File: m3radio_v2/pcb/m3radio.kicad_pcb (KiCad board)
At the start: 2 copper layers, 40 x 40 mm, 61 parts, among them IC1 NCP380, IC101 STM32F405RxTx, IC102 MCP2562, IC103 MAX-7Q, IC201 Si4460, J101 WEST TOP, J102 WEST BOT, J103 EAST TOP, J104 EAST BOT, P101 COAX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

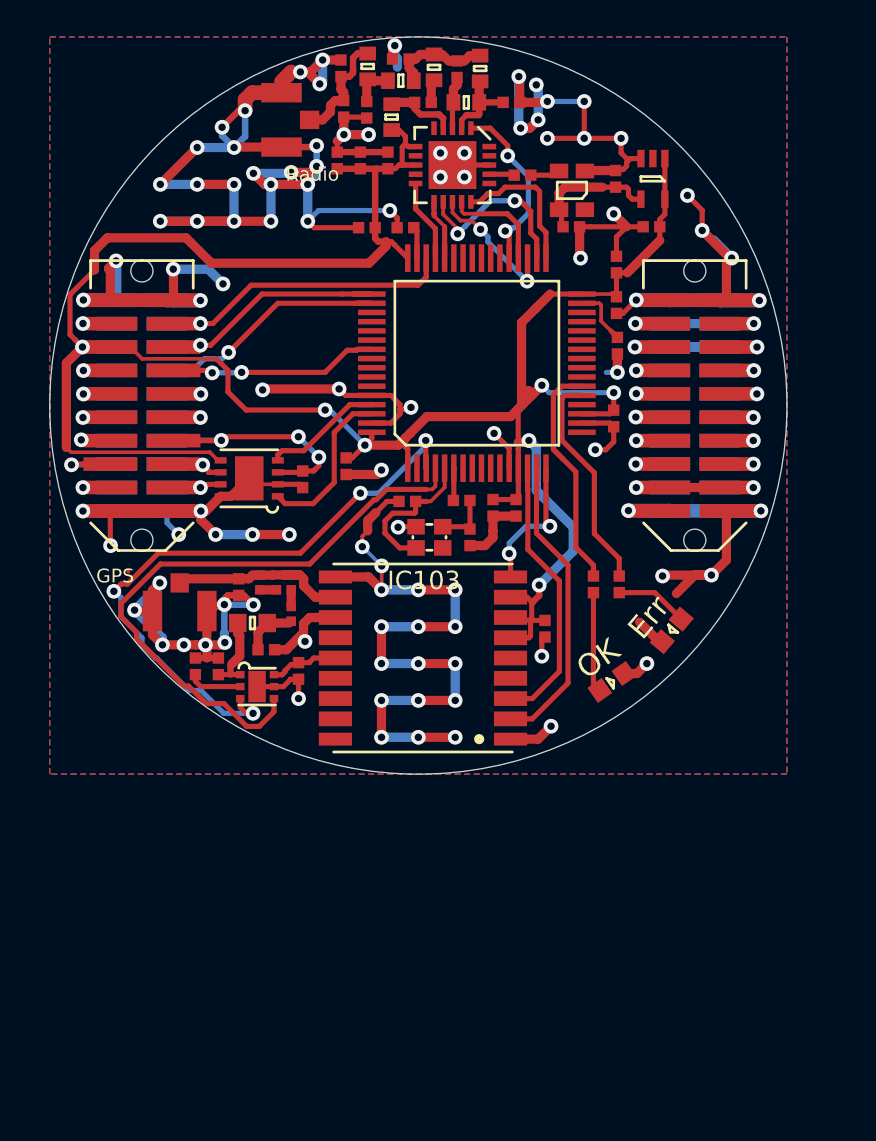
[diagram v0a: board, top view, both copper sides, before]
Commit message: Finish schematic, begin routing
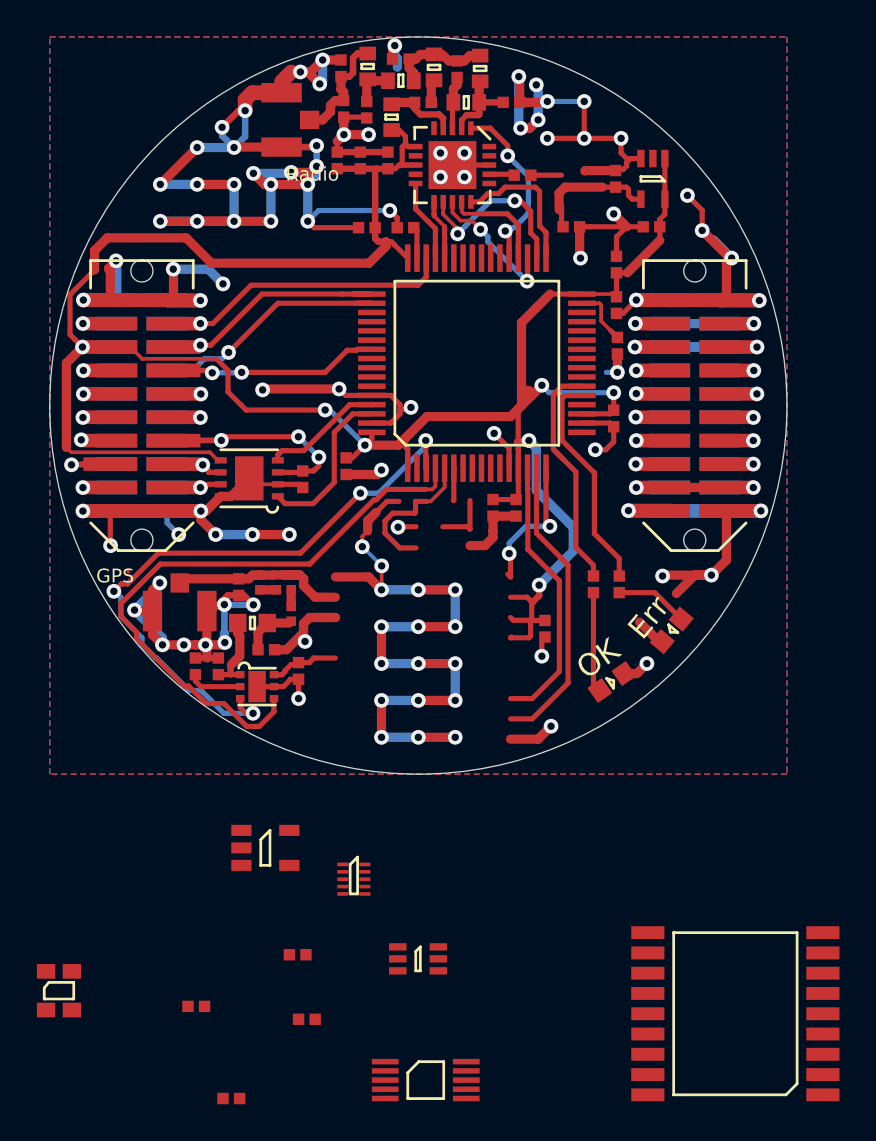
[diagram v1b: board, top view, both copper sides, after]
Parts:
- removed C101, C102: 10p, agg:0402
- removed IC103: MAX-7Q, M3radio:MAX-7Q
- removed R101: 100, agg:0402
- removed Y101: 26M, agg:XTAL-20x16
- removed Y201: TCXO, agg:TG-5006CG
- added C10: 100n, agg:0402, F.Cu at (93.5, 129.8)
- added C11: 1n, agg:0402, F.Cu at (94.0, 133.3)
- added C9: 100n, agg:0402, F.Cu at (89.8, 137.6)
- added IC2: NC7SZ04, agg:SOT-23-5, F.Cu at (91.7, 124.0)
- added IC3: CS2100-CP, agg:MSOP-10, F.Cu at (100.4, 136.6)
- added IC4: SL18860DC, agg:DFN-10-SL18860DC, F.Cu at (96.5, 125.7)
- added IC5: MAX_M8Q, agg:MAX-M8Q, F.Cu at (117.2, 133.0)
- added IC6: SN74LVC1G0832, agg:SC-70-6, F.Cu at (100.0, 130.0)
- added R3: 1M, agg:0402, F.Cu at (88.0, 132.6)
- added Y1: TCXO, agg:TG-5006CG, F.Cu at (80.5, 131.8)
- C1, C113: value 100nF -> 100n
- C106: value 1µ -> 1u
- C2, C3, C7, C8: value 1uF -> 1u
- C203: value 3pF -> 3p
- C204: value 36pF -> 36p
- C205: value 1.2pF -> 1.2p
- C206: value 3.3pF -> 3.3p
- C207: value 10pF -> 10p
- C208: value 4.7pF -> 4.7p
- C4: value 10nF -> 100n
- C5: value 100pF -> 1n
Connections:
- IC101 pad 2: Net-(IC101-Pad2) -> /GPS_PPS
- IC101 pad 29: Net-(IC101-Pad29) -> /PLL_SCL
- IC101 pad 30: Net-(IC101-Pad30) -> /PLL_SDA
- IC101 pad 33: /Radio/Radio_nSEL -> /Radio_nSEL
- IC101 pad 38: Net-(IC101-Pad38) -> /Radio_GATE
- IC101 pad 5: Net-(C101-Pad2) -> /STM_HSE
- IC201 pad 17: Net-(C5-Pad1) -> /Radio/Radio_XIN
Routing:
- net (no net): track 0.04 -> 44.0 mm, vias 0 -> 19
- net GND: track 329.0 -> 288.1 mm, vias 99 -> 80
- net Net-(C101-Pad2): track 8.06 -> 0.00 mm
- net /STM_HSE: track 0.00 -> 8.06 mm
- net Net-(C102-Pad1): track 3.08 -> 0.00 mm
- net /Radio_nSEL: track 0.00 -> 1.39 mm
- net /Radio/Radio_nSEL: track 7.92 -> 6.53 mm
- net Net-(C5-Pad1): track 1.37 -> 0.07 mm
- net /Radio/Radio_XIN: track 0.00 -> 1.30 mm

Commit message: Initial component placement (pcb)
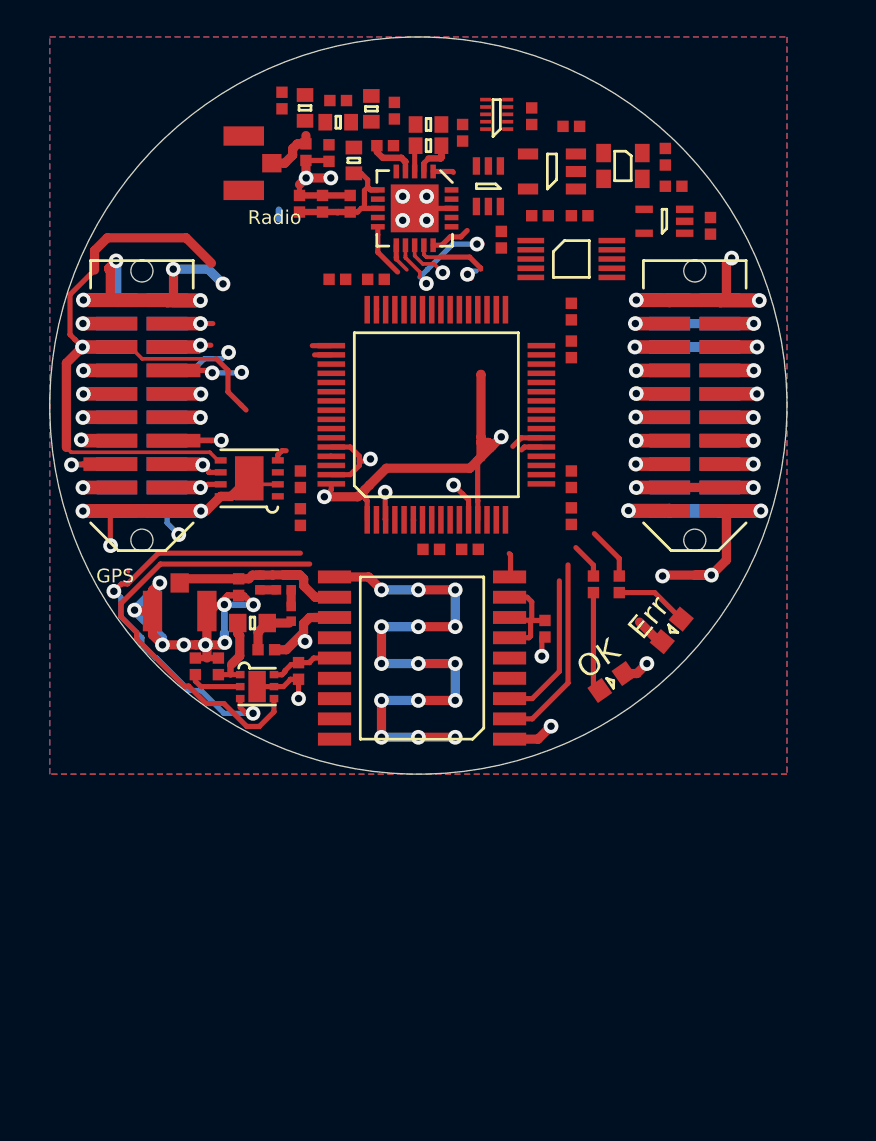
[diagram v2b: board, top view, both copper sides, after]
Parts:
- moved Y1 54.2 mm to (111.1, 87.0), turned to 270 degrees
- moved R3 51.9 mm to (108.3, 84.8), turned to 180 degrees
- moved C9 48.8 mm to (104.5, 91.0), turned to 270 degrees
- moved C10 47.2 mm to (106.2, 84.3), turned to 90 degrees
- moved C11 45.4 mm to (106.6, 89.7), turned to 180 degrees
- moved IC3 45.2 mm to (108.3, 92.0)
- moved IC4 42.2 mm to (104.2, 84.2), turned to 180 degrees
- moved IC6 42.1 mm to (103.8, 88.1), turned to 270 degrees
- moved IC2 39.9 mm to (107.2, 87.3), turned to 180 degrees
- moved IC5 25.7 mm to (100.2, 113.7)
- moved C103 13.9 mm to (108.3, 106.0), turned to 90 degrees
- moved C4 5.97 mm to (113.8, 88.1)
- moved L203 4.13 mm to (100.5, 84.8), turned to 180 degrees
- moved L206 4.08 mm to (93.8, 83.8)
- moved C205 4.08 mm to (98.7, 84.0)
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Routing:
- net GND: track 288.1 -> 194.4 mm, vias 80 -> 52
- net 3v3: track 139.0 -> 78.1 mm, vias 7 -> 3
- net (no net): track 44.0 -> 0.88 mm, vias 19 -> 1
- net /JTMS: track 17.6 -> 3.95 mm
- net /JTCK: track 13.5 -> 3.59 mm
- net /ANT_~EN: track 33.4 -> 23.9 mm
- net /LED_GRN: track 13.1 -> 3.68 mm
- net /ANT_~FLAG: track 34.4 -> 25.2 mm, vias 4 -> 3
- net /JTDI: track 14.3 -> 5.39 mm
- net /CAN_TXD: track 8.88 -> 0.00 mm
- net /Radio/Radio_SDN: track 9.81 -> 1.12 mm, vias 2 -> 0
- net /5v_CAN: track 14.2 -> 5.84 mm, vias 3 -> 1
- net /LED_RED: track 12.1 -> 4.00 mm
- net /STM_HSE: track 8.06 -> 0.00 mm
- net /JTDO: track 11.3 -> 3.76 mm
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
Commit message: Revise component placement
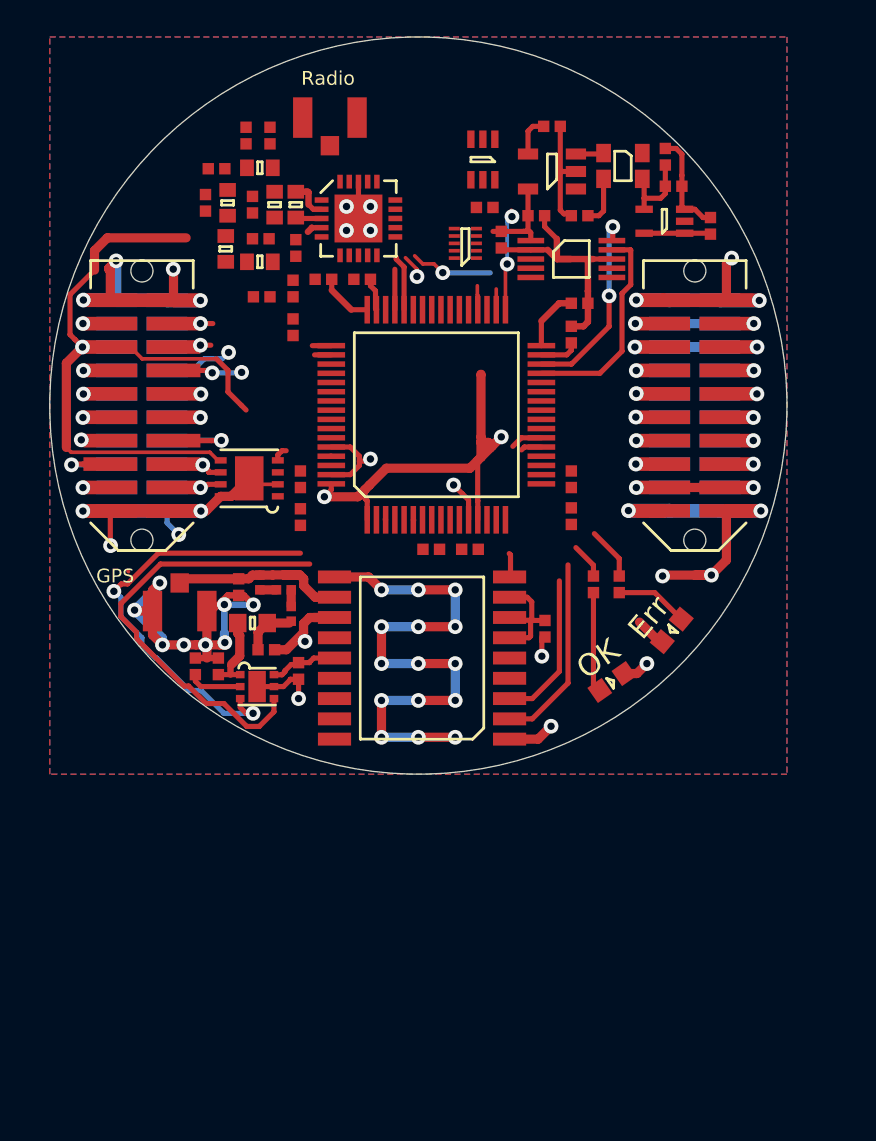
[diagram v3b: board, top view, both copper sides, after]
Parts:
- moved C203 12.0 mm to (91.0, 89.1)
- moved L204 10.3 mm to (91.4, 92.2), turned to 180 degrees
- moved C205 10.0 mm to (91.5, 91.0), turned to 180 degrees
- moved L203 9.42 mm to (92.2, 89.1), turned to 270 degrees
- moved C206 9.09 mm to (88.5, 89.0), turned to 90 degrees
- moved L201 8.45 mm to (89.5, 91.5), turned to 270 degrees
- moved L202 7.88 mm to (93.3, 89.1), turned to 90 degrees
- moved L205 7.43 mm to (89.7, 89.0), turned to 90 degrees
- moved C204 7.37 mm to (93.3, 91.5), turned to 270 degrees
- moved IC4 7.20 mm to (102.5, 91.2)
- moved C6 6.71 mm to (93.2, 95.8), turned to 270 degrees
- moved C207 6.16 mm to (89.0, 87.2), turned to 180 degrees
- moved C201 6.03 mm to (91.5, 94.1), turned to 180 degrees
- moved C10 5.57 mm to (103.6, 89.2), turned to 180 degrees
- moved C202 5.55 mm to (93.2, 93.7)
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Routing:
- net /PLL_SCL: track 0.00 -> 11.6 mm
- net /PLL_SDA: track 0.00 -> 10.8 mm, vias 0 -> 2
- net GND: track 194.4 -> 204.1 mm, vias 52 -> 49
- net Net-(C5-Pad1): track 0.00 -> 6.12 mm
- net /Radio_nSEL: track 0.00 -> 5.56 mm, vias 0 -> 2
- net 3v3: track 78.1 -> 83.6 mm
- net 1v8: track 0.00 -> 4.50 mm
- net /Radio/Radio_SCLK: track 6.22 -> 2.40 mm, vias 2 -> 1
- net Net-(C208-Pad1): track 2.94 -> 0.00 mm
- net Net-(C5-Pad2): track 0.00 -> 2.70 mm
- net /Radio/Radio_SDI: track 3.93 -> 1.31 mm
- net /Radio/TX_pin: track 2.78 -> 0.48 mm
- net Net-(IC2-Pad4): track 0.00 -> 2.20 mm
- net /Radio/Radio_nSEL: track 2.18 -> 0.00 mm
- net Net-(C111-Pad1): track 0.00 -> 2.13 mm
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
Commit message: Everthing seems to fit onto pcb, begin routing
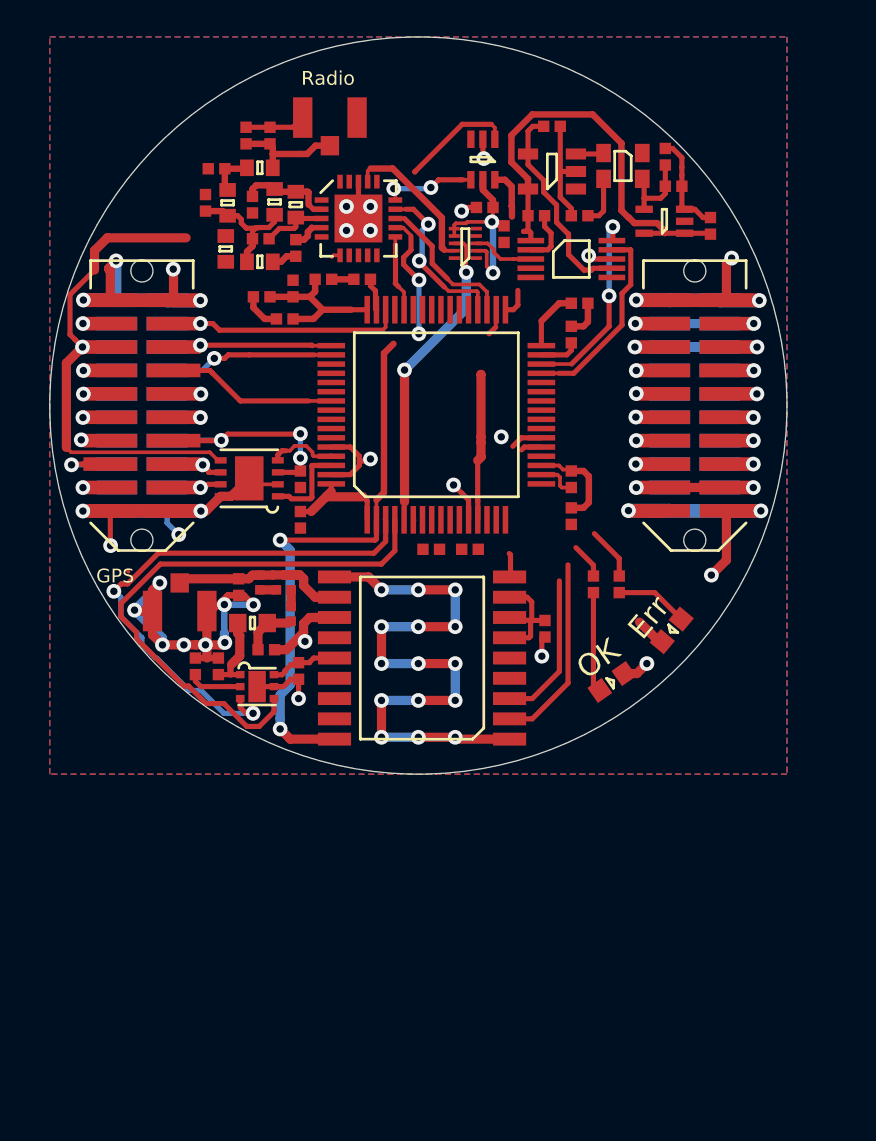
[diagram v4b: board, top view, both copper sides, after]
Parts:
- moved C6 0.64 mm to (92.8, 95.3), turned to 180 degrees
- moved C9 0.34 mm to (104.7, 90.7)
- moved C105 0.15 mm to (93.6, 106.2)
- moved L203 0.15 mm to (92.2, 89.0)
- turned C109 to 180 degrees
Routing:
- net /GPS_PPS: track 0.00 -> 36.2 mm, vias 0 -> 2
- net 3v3: track 83.6 -> 103.7 mm, vias 3 -> 4
- net /STM_HSE: track 0.00 -> 17.0 mm, vias 0 -> 2
- net /JTMS: track 3.95 -> 14.5 mm
- net Net-(IC2-Pad4): track 2.20 -> 11.3 mm
- net /Radio/Radio_SDI: track 1.31 -> 9.85 mm, vias 0 -> 2
- net /Radio/Radio_XIN: track 0.00 -> 8.11 mm
- net /5v_CAN: track 5.84 -> 13.3 mm, vias 1 -> 3
- net Net-(C205-Pad2): track 0.00 -> 6.80 mm
- net /Radio/Radio_SCLK: track 2.40 -> 9.01 mm, vias 1 -> 2
- net /ANT_~EN: track 23.9 -> 30.5 mm
- net /ANT_~FLAG: track 23.4 -> 29.5 mm
- net Net-(C208-Pad1): track 0.00 -> 5.95 mm
- net /JTCK: track 3.59 -> 9.10 mm
- net /JTDO: track 3.76 -> 9.25 mm, vias 2 -> 0
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
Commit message: Finish routing
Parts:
- moved C201 1.30 mm to (90.4, 94.8), turned to 270 degrees
- moved C202 1.15 mm to (93.2, 94.8), turned to 270 degrees
- moved C6 1.07 mm to (91.8, 94.8), turned to 270 degrees
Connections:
- IC101 pad 10: Net-(IC101-Pad10) -> (no net)
- IC101 pad 11: Net-(IC101-Pad11) -> (no net)
- IC101 pad 17: Net-(IC101-Pad17) -> (no net)
- IC101 pad 20: Net-(IC101-Pad20) -> (no net)
- IC101 pad 21: /LED_RED -> /LED_GRN
- IC101 pad 22: /LED_GRN -> /LED_RED
- IC101 pad 23: Net-(IC101-Pad23) -> (no net)
- IC101 pad 24: Net-(IC101-Pad24) -> (no net)
- IC101 pad 25: Net-(IC101-Pad25) -> (no net)
- IC101 pad 26: Net-(IC101-Pad26) -> (no net)
- IC101 pad 27: Net-(IC101-Pad27) -> (no net)
- IC101 pad 28: Net-(IC101-Pad28) -> (no net)
- IC101 pad 38: /Radio_GATE -> (no net)
- IC101 pad 39: Net-(IC101-Pad39) -> (no net)
- IC101 pad 40: Net-(IC101-Pad40) -> (no net)
- IC101 pad 41: Net-(IC101-Pad41) -> /Radio_GATE
- IC101 pad 42: Net-(IC101-Pad42) -> (no net)
- IC101 pad 43: Net-(IC101-Pad43) -> (no net)
- IC101 pad 51: Net-(IC101-Pad51) -> (no net)
- IC101 pad 52: Net-(IC101-Pad52) -> (no net)
- IC101 pad 53: Net-(IC101-Pad53) -> (no net)
- IC101 pad 54: Net-(IC101-Pad54) -> (no net)
- IC101 pad 56: Net-(IC101-Pad56) -> (no net)
- IC101 pad 57: Net-(IC101-Pad57) -> (no net)
- IC101 pad 58: Net-(IC101-Pad58) -> (no net)
- IC101 pad 59: Net-(IC101-Pad59) -> (no net)
- IC101 pad 6: Net-(IC101-Pad6) -> (no net)
- IC101 pad 7: Net-(IC101-Pad7) -> (no net)
- IC101 pad 8: Net-(IC101-Pad8) -> (no net)
- IC101 pad 9: Net-(IC101-Pad9) -> (no net)
- IC2 pad 1: Net-(IC2-Pad1) -> (no net)
- IC201 pad 16: Net-(IC201-Pad16) -> (no net)
- IC201 pad 19: Net-(IC201-Pad19) -> (no net)
- IC201 pad 20: Net-(IC201-Pad20) -> (no net)
- IC201 pad 5: Net-(IC201-Pad5) -> (no net)
- IC201 pad 7: Net-(IC201-Pad7) -> (no net)
- IC201 pad 9: Net-(IC201-Pad9) -> (no net)
- IC3 pad 4: Net-(IC3-Pad4) -> (no net)
- IC3 pad 6: Net-(IC3-Pad6) -> (no net)
- IC4 pad 10: Net-(IC4-Pad10) -> (no net)
- IC4 pad 4: Net-(IC4-Pad4) -> (no net)
- IC4 pad 5: Net-(IC4-Pad5) -> (no net)
- IC5 pad 13: Net-(IC5-Pad13) -> (no net)
- IC5 pad 15: Net-(IC5-Pad15) -> (no net)
- IC5 pad 16: Net-(IC5-Pad16) -> (no net)
- IC5 pad 17: Net-(IC5-Pad17) -> (no net)
- IC5 pad 5: Net-(IC5-Pad5) -> (no net)
- U1 pad 2: Net-(U1-Pad2) -> (no net)
- Y1 pad 1: Net-(Y1-Pad1) -> (no net)
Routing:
- net GND: track 203.9 -> 331.6 mm, vias 50 -> 107
- net 3v3: track 103.7 -> 162.0 mm, vias 4 -> 12
- net /GPS_TIM1: track 0.00 -> 26.8 mm
- net /Radio/Radio_SDN: track 0.00 -> 23.7 mm, vias 0 -> 2
- net /Radio_GATE: track 0.28 -> 10.6 mm, vias 0 -> 2
- net /GPS_PPS: track 36.2 -> 46.3 mm, vias 2 -> 4
- net /GPS_RX: track 8.18 -> 15.9 mm, vias 0 -> 2
- net /GPS_TX: track 10.3 -> 17.5 mm, vias 0 -> 2
- net /Radio/TX_pin: track 1.44 -> 8.54 mm
- net /LED_RED: track 4.00 -> 10.7 mm
- net /LED_GRN: track 3.68 -> 9.75 mm
- net /Radio/Radio_SCLK: track 9.01 -> 13.0 mm
- net /Radio_nSEL: track 4.65 -> 8.29 mm, vias 0 -> 2
- net /Radio/Radio_GPIO1: track 0.00 -> 3.35 mm
- net /GPS_RESET_N: track 1.51 -> 4.46 mm
